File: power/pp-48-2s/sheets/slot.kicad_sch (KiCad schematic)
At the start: 46 parts, among them J101 NODE, Q101 BSC070N10NS5, Q102 2N7002, Q103 2N7002, Q104 2N7002, U101 LM5069MM-2, U102 INA238AIDGSR, U103 74LVC1G74, U104 TLP176AM, U105 TLP176AM, U106 TLP291, X101 PM-19V-200W, X102 J2 AUX

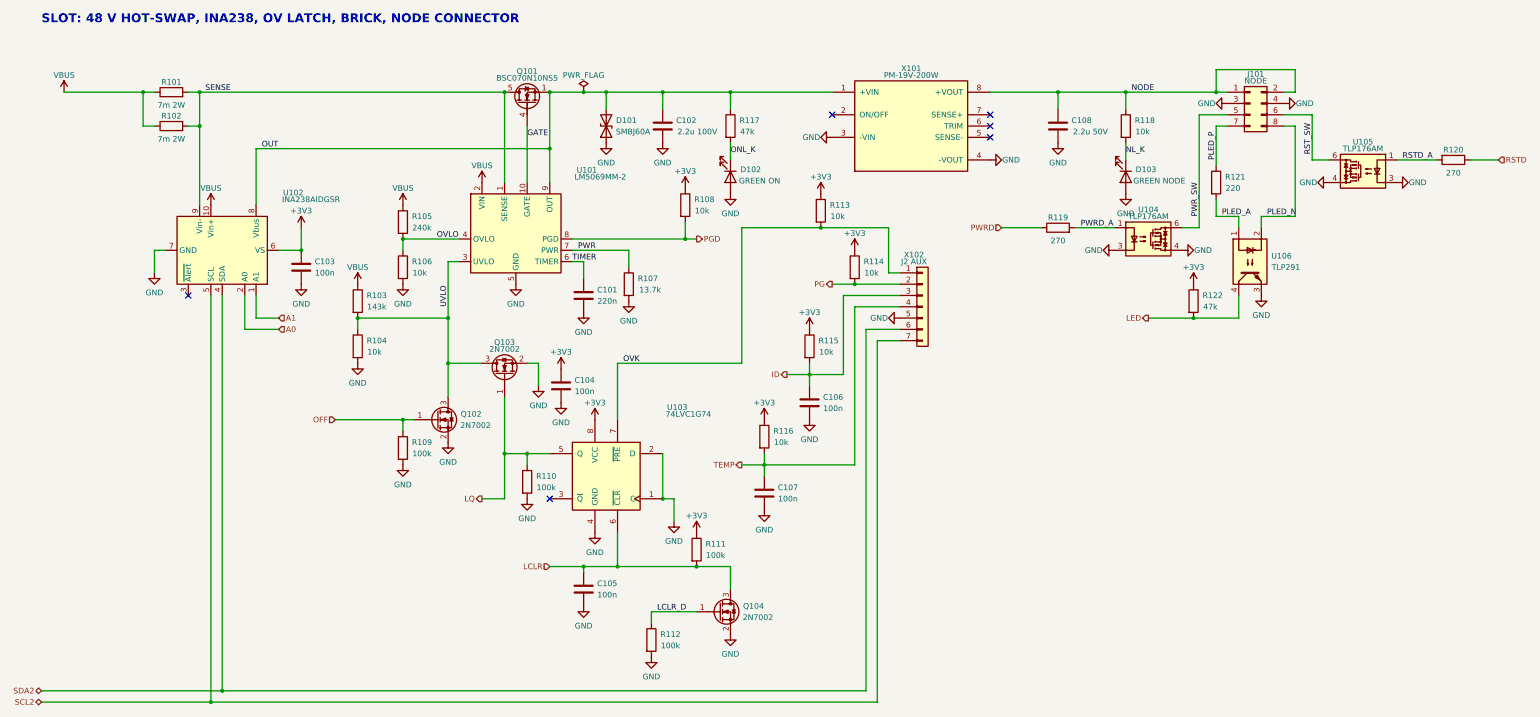
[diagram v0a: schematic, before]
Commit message: power: PP-48-2S four fixes: LED polarity, LM5164 ripple network, latch clear driver, brick sense checked
LEDs: Device:LED pin 1 is K; every LED had the resistor on pin 1 and
GND on pin 2. Nets swapped (LEDnn_K -> LEDnn_A), footprints turned 180
degrees (plan 80). Ripple injection: TI SNVSAU4D Table 6-1 / Fig 7-1
have CA node -> VOUT and CB node -> FB; tables fixed, C5/C6 and
C12/C13 swapped places and rewired on the board (plans 81, 82). Latch
clear: Sn_LCLR now drives the Q104/Q204 gate (+ R112/R212); the latch
node is /Slot n/CLRN (plans 81, 83). Brick SENSE+/-: the PM-19V-200W
module leaves pins 5-7 unconnected, X1.5/X1.7 stay NC.
ERC 0; schcheck shows exactly the intended pin changes; board relinked
with pcbkit relink --allow-shorts and hand-fixed; gndpour, silk,
connlabels re-run; DRC 5 warnings as before, 0 unconnected.
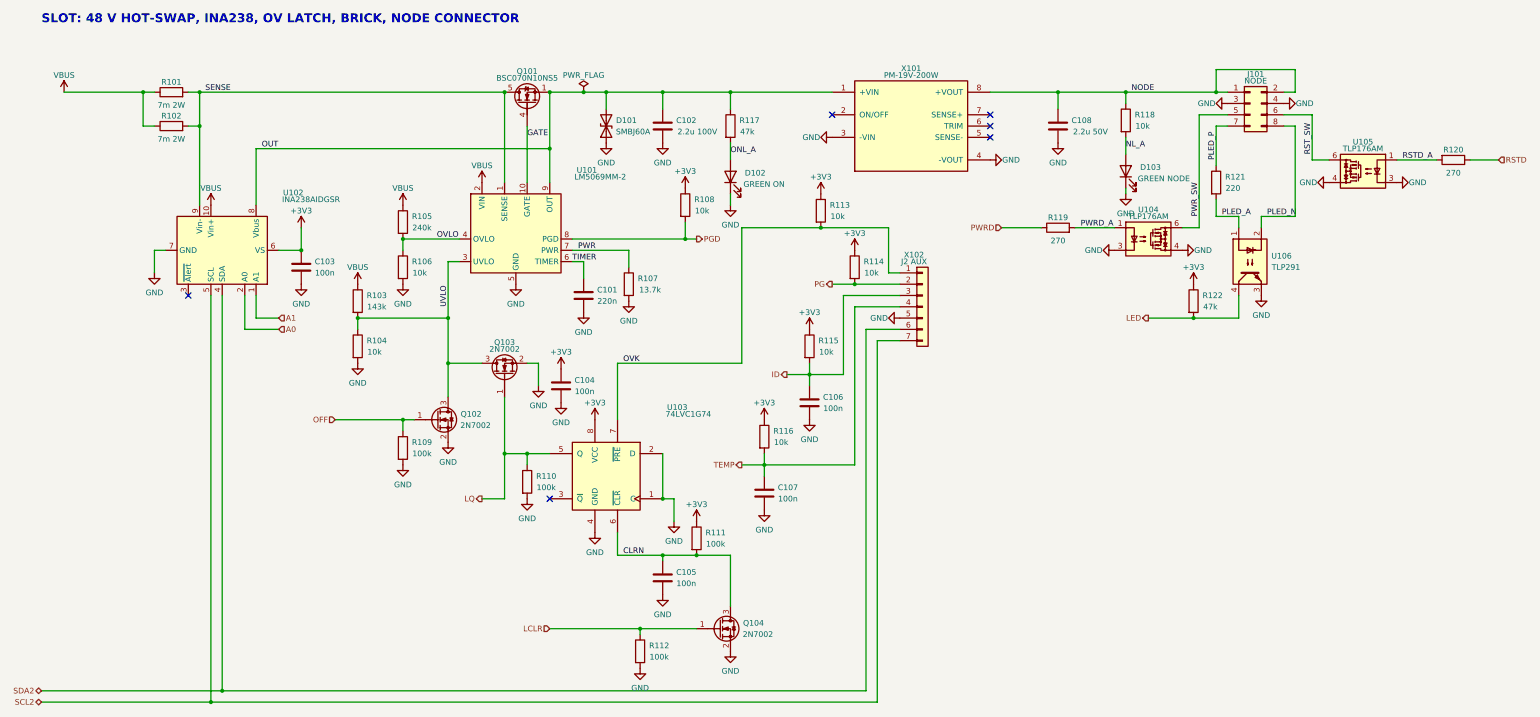
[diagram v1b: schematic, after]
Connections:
- net LCLR_D is gone; now on net LCLR: Q104.1 (G), R112.1
- net GND: now also D102.1 (K), D103.1 (K); no longer D102.2 (A), D103.2 (A)
- net LCLR: no longer C105.1, Q104.3 (D), R111.2, U103.6 (~{CLR})
- net NL_K renamed NL_A
- net NL_A: now also D103.2 (A); no longer D103.1 (K)
- net ONL_K renamed ONL_A
- net ONL_A: now also D102.2 (A); no longer D102.1 (K)
- new net CLRN: C105.1, Q104.3 (D), R111.2, U103.6 (~{CLR})
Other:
- moved on the sheet: C105, D102, D103, Q104, R111, R112, R118

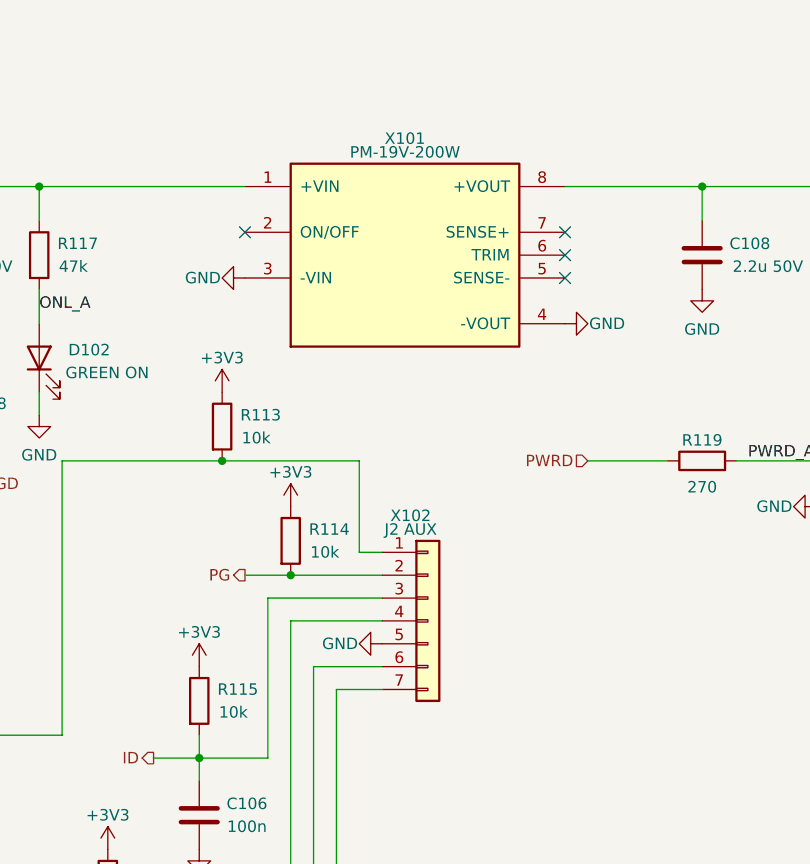
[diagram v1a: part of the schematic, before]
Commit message: power: screwed PM module mount footprints (M2 into SMT standoffs, pogo aux) on module, plane and bench carrier; RUN moves to aux pad 8; copper not yet rerouted
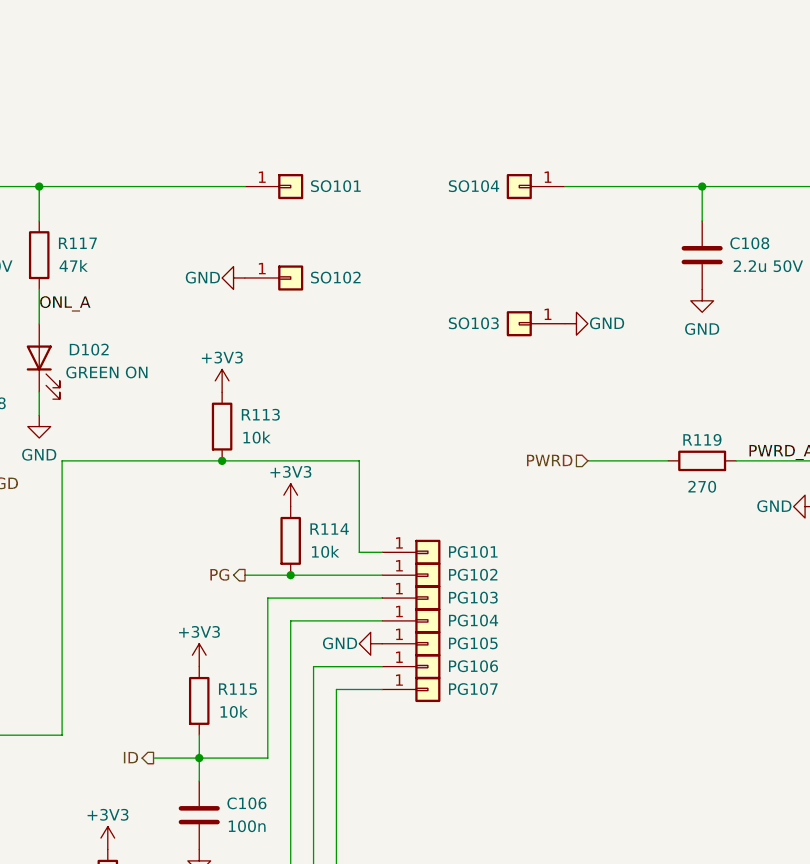
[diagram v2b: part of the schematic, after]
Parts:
- removed X101: PM-19V-200W, pp:Brick_Eighth_DOSA_Plane, symbol pp:PM_Brick_Socket
- removed X102: J2 AUX, Connector_PinHeader_1.27mm:PinHeader_1x07_P1.27mm_Vertical, symbol Connector_Generic:Conn_01x07
- added PG101, PG102, PG103, PG104, PG105, PG106, PG107: pogo, pp:PM_Pogo_YZ130115073P, symbol Connector_Generic:Conn_01x01
- added SO101, SO102, SO103, SO104: M2x6 standoff, pp:PM_Standoff_M2x6_SMTSO, symbol Connector_Generic:Conn_01x01
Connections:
- net GND: now also PG105.1 (Pin_1), SO102.1 (Pin_1), SO103.1 (Pin_1)
- net ID: now also PG103.1 (Pin_1)
- net NODE: now also SO104.1 (Pin_1)
- net OUT: now also SO101.1 (Pin_1)
- net OVK: now also PG101.1 (Pin_1)
- net PG: now also PG102.1 (Pin_1)
- net SCL2: now also PG107.1 (Pin_1)
- net SDA2: now also PG106.1 (Pin_1)
- net TEMP: now also PG104.1 (Pin_1)
- no-connect marks 6 -> 2

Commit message: Revert "power: screwed PM module mount footprints (M2 into SMT standoffs, pogo aux) on module, plane and bench carrier; RUN moves to aux pad 8; copper not yet rerouted"
This reverts commit abb9f50ba34d0b63e5425fa3cd376420f2890e7d.
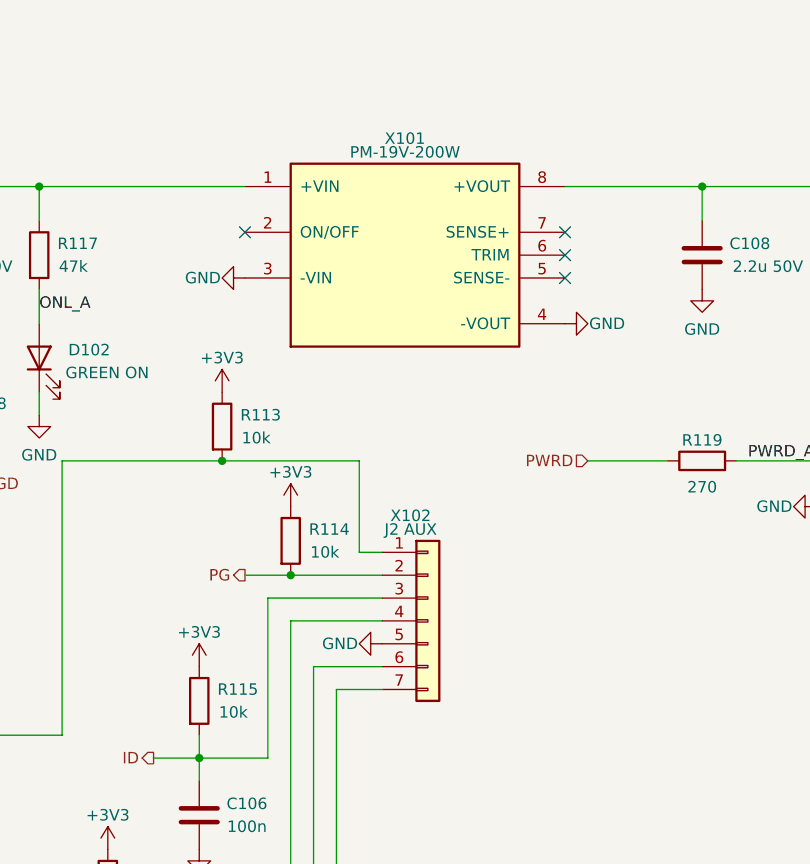
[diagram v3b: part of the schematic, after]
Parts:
- removed PG101, PG102, PG103, PG104, PG105, PG106, PG107: pogo, pp:PM_Pogo_YZ130115073P, symbol Connector_Generic:Conn_01x01
- removed SO101, SO102, SO103, SO104: M2x6 standoff, pp:PM_Standoff_M2x6_SMTSO, symbol Connector_Generic:Conn_01x01
- added X101: PM-19V-200W, pp:Brick_Eighth_DOSA_Plane, symbol pp:PM_Brick_Socket
- added X102: J2 AUX, Connector_PinHeader_1.27mm:PinHeader_1x07_P1.27mm_Vertical, symbol Connector_Generic:Conn_01x07
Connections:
- net GND: now also X101.3 (-VIN), X101.4 (-VOUT), X102.5 (Pin_5)
- net ID: now also X102.3 (Pin_3)
- net NODE: now also X101.8 (+VOUT)
- net OUT: now also X101.1 (+VIN)
- net OVK: now also X102.1 (Pin_1)
- net PG: now also X102.2 (Pin_2)
- net SCL2: now also X102.7 (Pin_7)
- net SDA2: now also X102.6 (Pin_6)
- net TEMP: now also X102.4 (Pin_4)
- no-connect marks 2 -> 6
